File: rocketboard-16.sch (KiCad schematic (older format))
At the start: 107 parts, among them J1 OLED, J2 SWD, K1 MX_RGB, K10 MX_RGB, K11 MX_RGB, K12 MX_RGB, K13 MX_RGB, K14 MX_RGB, K15 MX_RGB, K16 MX_RGB, K2 MX_RGB, K3 MX_RGB, K4 MX_RGB, K5 MX_RGB, K6 MX_RGB, K7 MX_RGB, K8 MX_RGB, K9 MX_RGB, P1 USB_C_Plug_USB2.0, SW1 SW_Push, SW2 Rotary 1, SW3 Rotary 2, U1 STM32F103C8T6, U2 AMS1117-3.3, U3 USBLC6-2SC6, X1 8 MHz, Y1 32.768 kHz

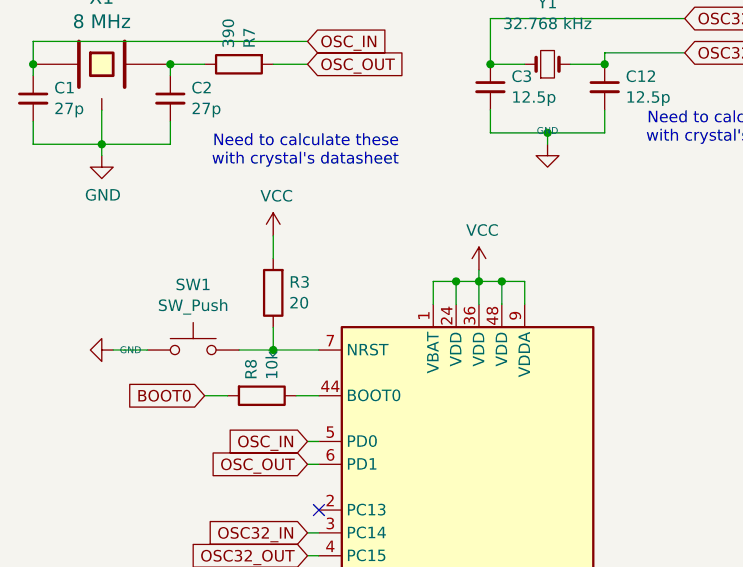
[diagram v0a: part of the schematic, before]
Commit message: Placed all componenets onto PCB and added josh's 3D model library in to get better 3D previews
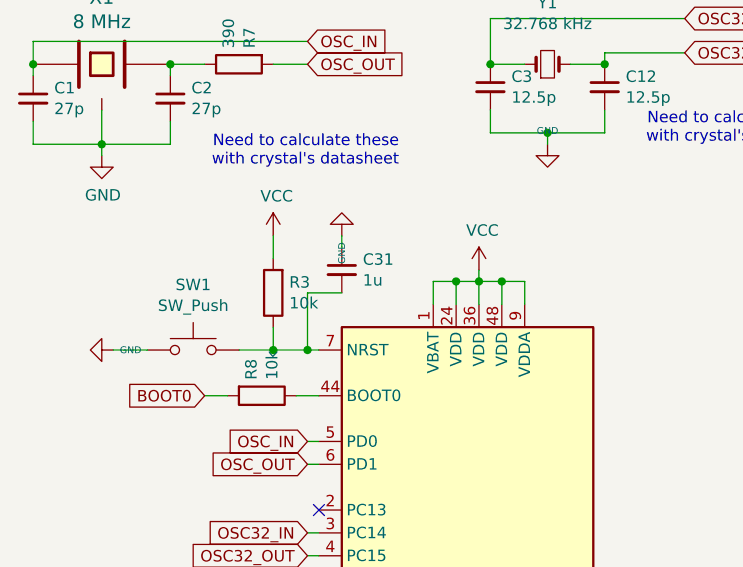
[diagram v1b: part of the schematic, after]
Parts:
- added C31: 1u, Capacitor_SMD:C_0603_1608Metric, symbol rocketboard-16-rescue:C_Small-Device-num_macro_pad-rescue
- C10, C13: footprint Capacitor_SMD:C_0603_1608Metric -> Capacitor_SMD:C_0805_2012Metric
- D20, D21, D22, D23, D24, D25, D26, D27, D28, D29, D30, D31, D32, D33, D34, D35: footprint josh-led:SK8612-MINI-E -> josh-keyboard:DUMMY_SK6812MINI-E
- R3: value 20 -> 10k
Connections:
- net GND: now also C31.1
- net at R3.1, SW1.2, U1.7 (NRST): now also C31.2
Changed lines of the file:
@@
 P 1650 1850
 F 0 "R3" H 1580 1804 50  0000 R CNN
-F 1 "20" H 1580 1895 50  0000 R CNN
+F 1 "10k" H 1580 1895 50  0000 R CNN
 F 2 "Resistor_SMD:R_0603_1608Metric" V 1580 1850 50  0001 C CNN
 F 3 "~" H 1650 1850 50  0001 C CNN
@@
 	1650 2100 1650 2000
 Wire Wire Line
-	1650 2100 1850 2100
+	1650 2100 1800 2100
 Connection ~ 1650 2100
 Wire Wire Line
@@
 F 0 "C13" H 4038 5646 50  0000 L CNN
 F 1 "10u" H 4038 5555 50  0000 L CNN
-F 2 "Capacitor_SMD:C_0603_1608Metric" H 3950 5600 50  0001 C CNN
+F 2 "Capacitor_SMD:C_0805_2012Metric" H 3950 5600 50  0001 C CNN
 F 3 "~" H 3950 5600 50  0001 C CNN
 	1    3950 5600
@@
 F 0 "C10" H 2838 5646 50  0000 L CNN
 F 1 "1u" H 2838 5555 50  0000 L CNN
-F 2 "Capacitor_SMD:C_0603_1608Metric" H 2750 5600 50  0001 C CNN
+F 2 "Capacitor_SMD:C_0805_2012Metric" H 2750 5600 50  0001 C CNN
 F 3 "~" H 2750 5600 50  0001 C CNN
 	1    2750 5600
@@
 F 0 "D20" H 9700 4496 50  0000 L CNN
 F 1 "SK6812MINI-E" H 9700 4405 50  0000 L CNN
-F 2 "josh-led:SK8612-MINI-E" H 9600 4450 50  0001 C CNN
+F 2 "josh-keyboard:DUMMY_SK6812MINI-E" H 9600 4450 50  0001 C CNN
 F 3 "~" H 9600 4450 50  0001 C CNN
 	1    9600 4450
@@
 F 0 "D21" H 9700 4696 50  0000 L CNN
 F 1 "SK6812MINI-E" H 9700 4605 50  0000 L CNN
-F 2 "josh-led:SK8612-MINI-E" H 9600 4650 50  0001 C CNN
+F 2 "josh-keyboard:DUMMY_SK6812MINI-E" H 9600 4650 50  0001 C CNN
 F 3 "~" H 9600 4650 50  0001 C CNN
 	1    9600 4650
@@
 F 0 "D22" H 9700 4896 50  0000 L CNN
 F 1 "SK6812MINI-E" H 9700 4805 50  0000 L CNN
-F 2 "josh-led:SK8612-MINI-E" H 9600 4850 50  0001 C CNN
+F 2 "josh-keyboard:DUMMY_SK6812MINI-E" H 9600 4850 50  0001 C CNN
 F 3 "~" H 9600 4850 50  0001 C CNN
 	1    9600 4850
@@
 F 0 "D23" H 9700 5096 50  0000 L CNN
 F 1 "SK6812MINI-E" H 9700 5005 50  0000 L CNN
-F 2 "josh-led:SK8612-MINI-E" H 9600 5050 50  0001 C CNN
+F 2 "josh-keyboard:DUMMY_SK6812MINI-E" H 9600 5050 50  0001 C CNN
 F 3 "~" H 9600 5050 50  0001 C CNN
 	1    9600 5050
@@
 F 0 "D24" H 9700 5296 50  0000 L CNN
 F 1 "SK6812MINI-E" H 9700 5205 50  0000 L CNN
-F 2 "josh-led:SK8612-MINI-E" H 9600 5250 50  0001 C CNN
+F 2 "josh-keyboard:DUMMY_SK6812MINI-E" H 9600 5250 50  0001 C CNN
 F 3 "~" H 9600 5250 50  0001 C CNN
 	1    9600 5250
@@
 F 0 "D25" H 9700 5496 50  0000 L CNN
 F 1 "SK6812MINI-E" H 9700 5405 50  0000 L CNN
-F 2 "josh-led:SK8612-MINI-E" H 9600 5450 50  0001 C CNN
+F 2 "josh-keyboard:DUMMY_SK6812MINI-E" H 9600 5450 50  0001 C CNN
 F 3 "~" H 9600 5450 50  0001 C CNN
 	1    9600 5450
@@
 F 0 "D26" H 9700 5696 50  0000 L CNN
 F 1 "SK6812MINI-E" H 9700 5605 50  0000 L CNN
-F 2 "josh-led:SK8612-MINI-E" H 9600 5650 50  0001 C CNN
+F 2 "josh-keyboard:DUMMY_SK6812MINI-E" H 9600 5650 50  0001 C CNN
 F 3 "~" H 9600 5650 50  0001 C CNN
 	1    9600 5650
@@
 F 0 "D27" H 9700 5896 50  0000 L CNN
 F 1 "SK6812MINI-E" H 9700 5805 50  0000 L CNN
-F 2 "josh-led:SK8612-MINI-E" H 9600 5850 50  0001 C CNN
+F 2 "josh-keyboard:DUMMY_SK6812MINI-E" H 9600 5850 50  0001 C CNN
 F 3 "~" H 9600 5850 50  0001 C CNN
 	1    9600 5850
@@
 F 0 "D28" H 10500 4496 50  0000 L CNN
 F 1 "SK6812MINI-E" H 10500 4405 50  0000 L CNN
-F 2 "josh-led:SK8612-MINI-E" H 10400 4450 50  0001 C CNN
+F 2 "josh-keyboard:DUMMY_SK6812MINI-E" H 10400 4450 50  0001 C CNN
 F 3 "~" H 10400 4450 50  0001 C CNN
 	1    10400 4450
@@
 F 0 "D29" H 10500 4696 50  0000 L CNN
 F 1 "SK6812MINI-E" H 10500 4605 50  0000 L CNN
-F 2 "josh-led:SK8612-MINI-E" H 10400 4650 50  0001 C CNN
+F 2 "josh-keyboard:DUMMY_SK6812MINI-E" H 10400 4650 50  0001 C CNN
 F 3 "~" H 10400 4650 50  0001 C CNN
 	1    10400 4650
@@
 F 0 "D30" H 10500 4896 50  0000 L CNN
 F 1 "SK6812MINI-E" H 10500 4805 50  0000 L CNN
-F 2 "josh-led:SK8612-MINI-E" H 10400 4850 50  0001 C CNN
+F 2 "josh-keyboard:DUMMY_SK6812MINI-E" H 10400 4850 50  0001 C CNN
 F 3 "~" H 10400 4850 50  0001 C CNN
 	1    10400 4850
@@
 F 0 "D31" H 10500 5096 50  0000 L CNN
 F 1 "SK6812MINI-E" H 10500 5005 50  0000 L CNN
-F 2 "josh-led:SK8612-MINI-E" H 10400 5050 50  0001 C CNN
+F 2 "josh-keyboard:DUMMY_SK6812MINI-E" H 10400 5050 50  0001 C CNN
 F 3 "~" H 10400 5050 50  0001 C CNN
 	1    10400 5050
@@
 F 0 "D32" H 10500 5296 50  0000 L CNN
 F 1 "SK6812MINI-E" H 10500 5205 50  0000 L CNN
-F 2 "josh-led:SK8612-MINI-E" H 10400 5250 50  0001 C CNN
+F 2 "josh-keyboard:DUMMY_SK6812MINI-E" H 10400 5250 50  0001 C CNN
 F 3 "~" H 10400 5250 50  0001 C CNN
 	1    10400 5250
@@
 F 0 "D33" H 10500 5496 50  0000 L CNN
 F 1 "SK6812MINI-E" H 10500 5405 50  0000 L CNN
-F 2 "josh-led:SK8612-MINI-E" H 10400 5450 50  0001 C CNN
+F 2 "josh-keyboard:DUMMY_SK6812MINI-E" H 10400 5450 50  0001 C CNN
 F 3 "~" H 10400 5450 50  0001 C CNN
 	1    10400 5450
@@
 F 0 "D34" H 10500 5696 50  0000 L CNN
 F 1 "SK6812MINI-E" H 10500 5605 50  0000 L CNN
-F 2 "josh-led:SK8612-MINI-E" H 10400 5650 50  0001 C CNN
+F 2 "josh-keyboard:DUMMY_SK6812MINI-E" H 10400 5650 50  0001 C CNN
 F 3 "~" H 10400 5650 50  0001 C CNN
 	1    10400 5650
@@
 F 0 "D35" H 10500 5896 50  0000 L CNN
 F 1 "SK6812MINI-E" H 10500 5805 50  0000 L CNN
-F 2 "josh-led:SK8612-MINI-E" H 10400 5850 50  0001 C CNN
+F 2 "josh-keyboard:DUMMY_SK6812MINI-E" H 10400 5850 50  0001 C CNN
 F 3 "~" H 10400 5850 50  0001 C CNN
 	1    10400 5850
@@
 Wire Wire Line
 	1750 5500 1850 5500
+$Comp
+L rocketboard-16-rescue:C_Small-Device-num_macro_pad-rescue C31
+U 1 1 5F723709
+P 1950 1750
+F 0 "C31" H 2042 1796 50  0000 L CNN
+F 1 "1u" H 2042 1705 50  0000 L CNN
+F 2 "Capacitor_SMD:C_0603_1608Metric" H 1950 1750 50  0001 C CNN
+F 3 "~" H 1950 1750 50  0001 C CNN
+	1    1950 1750
+	1    0    0    -1
+$EndComp
+$Comp
+L power:GND #PWR061
+U 1 1 5F73FA85
+P 1950 1600
+F 0 "#PWR061" H 1950 1650 20  0001 C CNN
+F 1 "GND" V 1950 1629 30  0000 L CNN
+F 2 "" H 1950 1600 60  0000 C CNN
+F 3 "" H 1950 1600 60  0000 C CNN
+	1    1950 1600
+	-1   0    0    1
+$EndComp
+Wire Wire Line
+	1950 1600 1950 1650
+Wire Wire Line
+	1950 1850 1800 1850
+Wire Wire Line
+	1800 1850 1800 2100
+Connection ~ 1800 2100
+Wire Wire Line
+	1800 2100 1850 2100
 $EndSCHEMATC

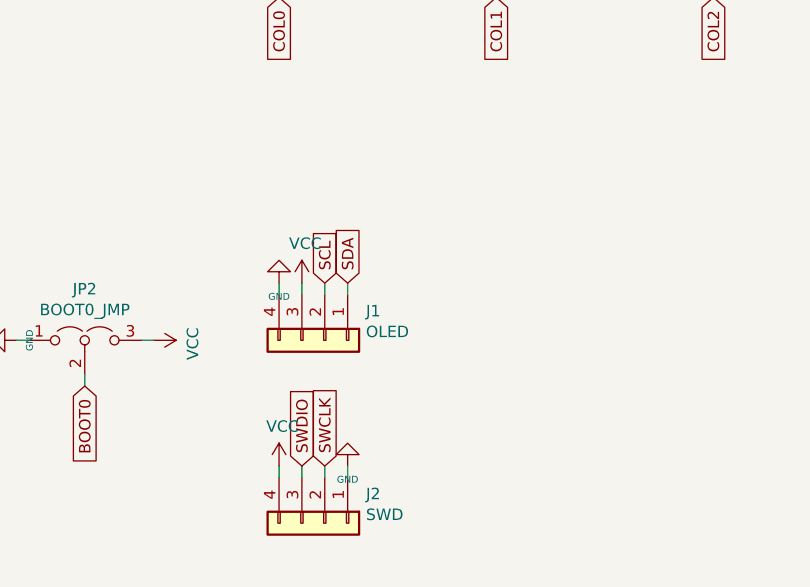
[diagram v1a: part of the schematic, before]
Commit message: Fixed some of the 3D model references, added a symbol/footprint for the SSD1306 OLED display with a 3D model for pictures, and added draft logo with board info
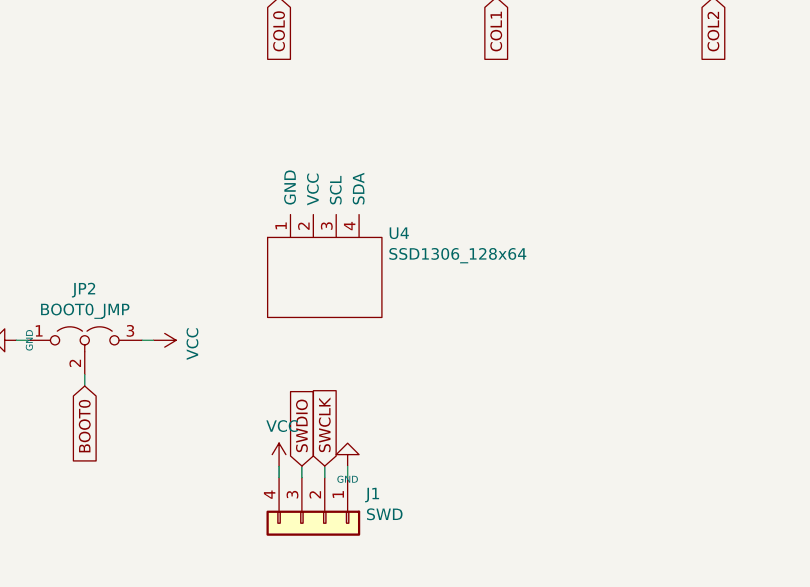
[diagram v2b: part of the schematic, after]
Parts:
- removed J1: OLED, Connector_PinHeader_2.54mm:PinHeader_1x04_P2.54mm_Vertical, symbol rocketboard-16-rescue:Conn_01x04-Connector_Generic-num_macro_pad-rescue
- added U4: SSD1306_128x64, Connector_PinHeader_2.54mm:PinHeader_1x04_P2.54mm_Vertical, symbol seth-display:SSD1306_128x64
- K1, K10, K11, K12, K13, K14, K15, K16, K2, K3, K4, K5, K6, K7, K8, K9: footprint josh-keyboard:MX_KEYSWITCH_RGB -> josh-keyboard:MX_KEYSWITCH_RGB_2D
- SW2, SW3: footprint Rotary_Encoder:RotaryEncoder_Alps_EC11E-Switch_Vertical_H20mm -> josh-buttons-switches:RotaryEncoder_Alps_EC11E-Switch_Vertical_H20mm_CircularMountingHoles
- renumbered J2 to J1
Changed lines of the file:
@@
 	1    0    0    -1
-$EndComp
-Text GLabel 6400 6500 1    50   Input ~ 0
-SDA
-Text GLabel 6300 6500 1    50   Input ~ 0
-SCL
-$Comp
-L rocketboard-16-rescue:VCC-power-num_macro_pad-rescue #PWR017
-U 1 1 5F4E5742
-P 6200 6500
-F 0 "#PWR017" H 6200 6350 50  0001 C CNN
-F 1 "VCC" H 6215 6673 50  0000 C CNN
-F 2 "" H 6200 6500 50  0001 C CNN
-F 3 "" H 6200 6500 50  0001 C CNN
-	1    6200 6500
-	1    0    0    -1
-$EndComp
-$Comp
-L power:GND #PWR015
-U 1 1 5F4E6576
-P 6100 6500
-F 0 "#PWR015" H 6100 6550 20  0001 C CNN
-F 1 "GND" H 6100 6559 30  0000 C CNN
-F 2 "" H 6100 6500 60  0000 C CNN
-F 3 "" H 6100 6500 60  0000 C CNN
-	1    6100 6500
-	-1   0    0    1
 $EndComp
 Text GLabel 1800 4400 0    50   Input ~ 0
@@
 SWCLK
 $Comp
-L rocketboard-16-rescue:Conn_01x04-Connector_Generic-num_macro_pad-rescue J2
+L rocketboard-16-rescue:Conn_01x04-Connector_Generic-num_macro_pad-rescue J1
 U 1 1 5F3D89F3
 P 6300 7550
-F 0 "J2" V 6172 7730 50  0000 L CNN
+F 0 "J1" V 6172 7730 50  0000 L CNN
 F 1 "SWD" V 6263 7730 50  0000 L CNN
 F 2 "Connector_PinHeader_2.54mm:PinHeader_1x04_P2.54mm_Vertical" H 6300 7550 50  0001 C CNN
@@
 Text Notes 2200 1300 2    50   ~ 0
 Need to calculate these \nwith crystal's datasheet\n
-$Comp
-L rocketboard-16-rescue:Conn_01x04-Connector_Generic-num_macro_pad-rescue J1
-U 1 1 5F4DBEB2
-P 6300 6750
-F 0 "J1" V 6172 6930 50  0000 L CNN
-F 1 "OLED" V 6263 6930 50  0000 L CNN
-F 2 "Connector_PinHeader_2.54mm:PinHeader_1x04_P2.54mm_Vertical" H 6300 6750 50  0001 C CNN
-F 3 "~" H 6300 6750 50  0001 C CNN
-	1    6300 6750
-	0    1    1    0
-$EndComp
 $Comp
 L rocketboard-16-rescue:C_Small-Device-num_macro_pad-rescue C14
@@
 F 0 "SW3" V 9296 820 50  0000 R CNN
 F 1 "Rotary 2" V 9205 820 50  0000 R CNN
-F 2 "Rotary_Encoder:RotaryEncoder_Alps_EC11E-Switch_Vertical_H20mm" H 9100 1210 50  0001 C CNN
+F 2 "josh-buttons-switches:RotaryEncoder_Alps_EC11E-Switch_Vertical_H20mm_CircularMountingHoles" H 9100 1210 50  0001 C CNN
 F 3 "~" H 9250 1310 50  0001 C CNN
 	1    9250 1050
@@
 F 0 "SW2" V 5746 820 50  0000 R CNN
 F 1 "Rotary 1" V 5655 820 50  0000 R CNN
-F 2 "Rotary_Encoder:RotaryEncoder_Alps_EC11E-Switch_Vertical_H20mm" H 5550 1210 50  0001 C CNN
+F 2 "josh-buttons-switches:RotaryEncoder_Alps_EC11E-Switch_Vertical_H20mm_CircularMountingHoles" H 5550 1210 50  0001 C CNN
 F 3 "~" H 5700 1310 50  0001 C CNN
 	1    5700 1050
@@
 F 0 "K2" H 6600 2825 50  0000 C CNN
 F 1 "MX_RGB" H 6600 2734 50  0000 C CNN
-F 2 "josh-keyboard:MX_KEYSWITCH_RGB" H 6600 2450 50  0001 C CNN
+F 2 "josh-keyboard:MX_KEYSWITCH_RGB_2D" H 6600 2450 50  0001 C CNN
 F 3 "~" H 6600 2450 50  0001 C CNN
 	1    6600 2250
@@
 F 0 "K3" H 7550 2825 50  0000 C CNN
 F 1 "MX_RGB" H 7550 2734 50  0000 C CNN
-F 2 "josh-keyboard:MX_KEYSWITCH_RGB" H 7550 2450 50  0001 C CNN
+F 2 "josh-keyboard:MX_KEYSWITCH_RGB_2D" H 7550 2450 50  0001 C CNN
 F 3 "~" H 7550 2450 50  0001 C CNN
 	1    7550 2250
@@
 F 0 "K4" H 8500 2825 50  0000 C CNN
 F 1 "MX_RGB" H 8500 2734 50  0000 C CNN
-F 2 "josh-keyboard:MX_KEYSWITCH_RGB" H 8500 2450 50  0001 C CNN
+F 2 "josh-keyboard:MX_KEYSWITCH_RGB_2D" H 8500 2450 50  0001 C CNN
 F 3 "~" H 8500 2450 50  0001 C CNN
 	1    8500 2250
@@
 F 0 "K5" H 5650 3675 50  0000 C CNN
 F 1 "MX_RGB" H 5650 3584 50  0000 C CNN
-F 2 "josh-keyboard:MX_KEYSWITCH_RGB" H 5650 3300 50  0001 C CNN
+F 2 "josh-keyboard:MX_KEYSWITCH_RGB_2D" H 5650 3300 50  0001 C CNN
 F 3 "~" H 5650 3300 50  0001 C CNN
 	1    5650 3100
@@
 F 0 "K6" H 6600 3675 50  0000 C CNN
 F 1 "MX_RGB" H 6600 3584 50  0000 C CNN
-F 2 "josh-keyboard:MX_KEYSWITCH_RGB" H 6600 3300 50  0001 C CNN
+F 2 "josh-keyboard:MX_KEYSWITCH_RGB_2D" H 6600 3300 50  0001 C CNN
 F 3 "~" H 6600 3300 50  0001 C CNN
 	1    6600 3100
@@
 F 0 "K7" H 7550 3675 50  0000 C CNN
 F 1 "MX_RGB" H 7550 3584 50  0000 C CNN
-F 2 "josh-keyboard:MX_KEYSWITCH_RGB" H 7550 3300 50  0001 C CNN
+F 2 "josh-keyboard:MX_KEYSWITCH_RGB_2D" H 7550 3300 50  0001 C CNN
 F 3 "~" H 7550 3300 50  0001 C CNN
 	1    7550 3100
@@
 F 0 "K8" H 8500 3675 50  0000 C CNN
 F 1 "MX_RGB" H 8500 3584 50  0000 C CNN
-F 2 "josh-keyboard:MX_KEYSWITCH_RGB" H 8500 3300 50  0001 C CNN
+F 2 "josh-keyboard:MX_KEYSWITCH_RGB_2D" H 8500 3300 50  0001 C CNN
 F 3 "~" H 8500 3300 50  0001 C CNN
 	1    8500 3100
@@
 F 0 "K9" H 5650 4525 50  0000 C CNN
 F 1 "MX_RGB" H 5650 4434 50  0000 C CNN
-F 2 "josh-keyboard:MX_KEYSWITCH_RGB" H 5650 4150 50  0001 C CNN
+F 2 "josh-keyboard:MX_KEYSWITCH_RGB_2D" H 5650 4150 50  0001 C CNN
 F 3 "~" H 5650 4150 50  0001 C CNN
 	1    5650 3950
@@
 F 0 "K10" H 6600 4525 50  0000 C CNN
 F 1 "MX_RGB" H 6600 4434 50  0000 C CNN
-F 2 "josh-keyboard:MX_KEYSWITCH_RGB" H 6600 4150 50  0001 C CNN
+F 2 "josh-keyboard:MX_KEYSWITCH_RGB_2D" H 6600 4150 50  0001 C CNN
 F 3 "~" H 6600 4150 50  0001 C CNN
 	1    6600 3950
@@
 F 0 "K11" H 7550 4525 50  0000 C CNN
 F 1 "MX_RGB" H 7550 4434 50  0000 C CNN
-F 2 "josh-keyboard:MX_KEYSWITCH_RGB" H 7550 4150 50  0001 C CNN
+F 2 "josh-keyboard:MX_KEYSWITCH_RGB_2D" H 7550 4150 50  0001 C CNN
 F 3 "~" H 7550 4150 50  0001 C CNN
 	1    7550 3950
@@
 F 0 "K12" H 8500 4525 50  0000 C CNN
 F 1 "MX_RGB" H 8500 4434 50  0000 C CNN
-F 2 "josh-keyboard:MX_KEYSWITCH_RGB" H 8500 4150 50  0001 C CNN
+F 2 "josh-keyboard:MX_KEYSWITCH_RGB_2D" H 8500 4150 50  0001 C CNN
 F 3 "~" H 8500 4150 50  0001 C CNN
 	1    8500 3950
@@
 F 0 "K13" H 5650 5375 50  0000 C CNN
 F 1 "MX_RGB" H 5650 5284 50  0000 C CNN
-F 2 "josh-keyboard:MX_KEYSWITCH_RGB" H 5650 5000 50  0001 C CNN
+F 2 "josh-keyboard:MX_KEYSWITCH_RGB_2D" H 5650 5000 50  0001 C CNN
 F 3 "~" H 5650 5000 50  0001 C CNN
 	1    5650 4800
@@
 F 0 "K14" H 6600 5375 50  0000 C CNN
 F 1 "MX_RGB" H 6600 5284 50  0000 C CNN
-F 2 "josh-keyboard:MX_KEYSWITCH_RGB" H 6600 5000 50  0001 C CNN
+F 2 "josh-keyboard:MX_KEYSWITCH_RGB_2D" H 6600 5000 50  0001 C CNN
 F 3 "~" H 6600 5000 50  0001 C CNN
 	1    6600 4800
@@
 F 0 "K15" H 7550 5375 50  0000 C CNN
 F 1 "MX_RGB" H 7550 5284 50  0000 C CNN
-F 2 "josh-keyboard:MX_KEYSWITCH_RGB" H 7550 5000 50  0001 C CNN
+F 2 "josh-keyboard:MX_KEYSWITCH_RGB_2D" H 7550 5000 50  0001 C CNN
 F 3 "~" H 7550 5000 50  0001 C CNN
 	1    7550 4800
@@
 F 0 "K16" H 8500 5375 50  0000 C CNN
 F 1 "MX_RGB" H 8500 5284 50  0000 C CNN
-F 2 "josh-keyboard:MX_KEYSWITCH_RGB" H 8500 5000 50  0001 C CNN
+F 2 "josh-keyboard:MX_KEYSWITCH_RGB_2D" H 8500 5000 50  0001 C CNN
 F 3 "~" H 8500 5000 50  0001 C CNN
 	1    8500 4800
@@
 F 0 "K1" H 5650 2825 50  0000 C CNN
 F 1 "MX_RGB" H 5650 2734 50  0000 C CNN
-F 2 "josh-keyboard:MX_KEYSWITCH_RGB" H 5650 2450 50  0001 C CNN
+F 2 "josh-keyboard:MX_KEYSWITCH_RGB_2D" H 5650 2450 50  0001 C CNN
 F 3 "~" H 5650 2450 50  0001 C CNN
 	1    5650 2250
@@
 	5500 6750 5550 6750
 Wire Wire Line
-	6100 6500 6100 6550
-Wire Wire Line
-	6200 6500 6200 6550
-Wire Wire Line
-	6300 6500 6300 6550
-Wire Wire Line
-	6400 6500 6400 6550
-Wire Wire Line
 	6100 7300 6100 7350
 Wire Wire Line
@@
 Wire Wire Line
 	1800 2100 1850 2100
+$Comp
+L seth-display:SSD1306_128x64 U4
+U 1 1 5F6740EF
+P 6300 6450
+F 0 "U4" H 6578 6617 50  0000 L CNN
+F 1 "SSD1306_128x64" H 6578 6526 50  0000 L CNN
+F 2 "Connector_PinHeader_2.54mm:PinHeader_1x04_P2.54mm_Vertical" H 5950 6400 50  0001 C CNN
+F 3 "" H 5950 6400 50  0001 C CNN
+	1    6300 6450
+	1    0    0    -1
+$EndComp
 $EndSCHEMATC

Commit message: Routed most of the wires, many still needed though. Changed a couple of pins around on the schematic due to simpler routing paths.
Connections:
- net GND: now also U4.1 (GND)
- net ROW0: now also U1.30 (PA9); no longer U1.25 (PB12)
- net Row4: now also U1.39 (PB3); no longer U1.13 (PA3)
- net SCL: now also U4.3 (SCL)
- net SDA: now also U4.4 (SDA)
- net VCC: now also U4.2 (VCC)
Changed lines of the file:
@@
 	1    0    0    -1
 $EndComp
-Text GLabel 1800 4400 0    50   Input ~ 0
+Text GLabel 3150 4100 2    50   Input ~ 0
 ROW0
 Text GLabel 1800 4500 0    50   Input ~ 0
@@
 NoConn ~ 1850 3200
 NoConn ~ 1850 3300
-NoConn ~ 1850 3500
 NoConn ~ 1850 3600
 NoConn ~ 1850 3700
 NoConn ~ 3150 4700
 NoConn ~ 3150 4200
-NoConn ~ 3150 4100
 NoConn ~ 3150 4000
 NoConn ~ 3150 3700
@@
 Text GLabel 5200 5100 0    50   Input ~ 0
 Row4
-Text GLabel 3200 3500 2    50   Input ~ 0
+Text GLabel 1850 3500 0    50   Input ~ 0
 Row4
 Wire Wire Line
@@
 	1850 4300 1800 4300
 Wire Wire Line
-	1800 4400 1850 4400
-Wire Wire Line
 	1850 4500 1800 4500
 Wire Wire Line
@@
 Wire Wire Line
 	3200 3400 3150 3400
-Wire Wire Line
-	3150 3500 3200 3500
 Wire Wire Line
 	3200 3800 3150 3800
@@
 	1    0    0    -1
 $EndComp
+$Comp
+L power:GND #PWR0102
+U 1 1 5F67F142
+P 6150 5900
+F 0 "#PWR0102" H 6150 5950 20  0001 C CNN
+F 1 "GND" H 6150 5959 30  0000 C CNN
+F 2 "" H 6150 5900 60  0000 C CNN
+F 3 "" H 6150 5900 60  0000 C CNN
+	1    6150 5900
+	-1   0    0    1
+$EndComp
+$Comp
+L rocketboard-16-rescue:VCC-power-num_macro_pad-rescue #PWR0103
+U 1 1 5F69BED7
+P 6250 5900
+F 0 "#PWR0103" H 6250 5750 50  0001 C CNN
+F 1 "VCC" H 6265 6073 50  0000 C CNN
+F 2 "" H 6250 5900 50  0001 C CNN
+F 3 "" H 6250 5900 50  0001 C CNN
+	1    6250 5900
+	1    0    0    -1
+$EndComp
+Text GLabel 6350 5900 1    50   Input ~ 0
+SCL
+Text GLabel 6450 5900 1    50   Input ~ 0
+SDA
+Wire Wire Line
+	6150 6300 6150 5900
+Wire Wire Line
+	6250 6300 6250 5900
+Wire Wire Line
+	6350 5900 6350 6300
+Wire Wire Line
+	6450 6300 6450 5900
+NoConn ~ 3150 3500
+NoConn ~ 1850 4400
 $EndSCHEMATC
